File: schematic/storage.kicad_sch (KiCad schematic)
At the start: 0 parts

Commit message: revised schematic into sheets for easier design. Looks much better.
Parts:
- added JP1, JP2: SolderJumper_2_Open, symbol Jumper:SolderJumper_2_Open
- added U2: 27C256, Package_DIP:DIP-28_W15.24mm, symbol Memory_EPROM:27C256
- added U3, U4: SCM2114AL, symbol Vintage_PC_RAM:SCM2114AL
- added WJ4, WJ5: Jumper_2_Bridged_32K_ROM, symbol Jumper:Jumper_2_Bridged
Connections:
- new net: JP2.2 (B), U2.23 (A11), WJ5.2 (B)
- new net: JP1.1 (A), U2.20 (~{CE}), WJ4.1 (A)
- new net +5VD: U2.1 (VPP), U2.26 (A13), U2.27 (A14), U2.28 (VCC), U3.18 (VCC), U4.18 (VCC)
- new net A11: JP1.2 (B), WJ5.1 (A)
- new net A12: JP2.1 (A), U2.2 (A12)
- new net D0: U2.11 (D0)
- new net D1: U2.12 (D1)
- new net D2: U2.13 (D2)
- new net D3: U2.15 (D3)
- new net D4: U2.16 (D4), U4.14 (D0)
- new net D5: U2.17 (D5)
- new net D6: U2.18 (D6)
- new net D7: U2.19 (D7)
- new net U5_O0: U2.22 (~{OE}), WJ4.2 (B)

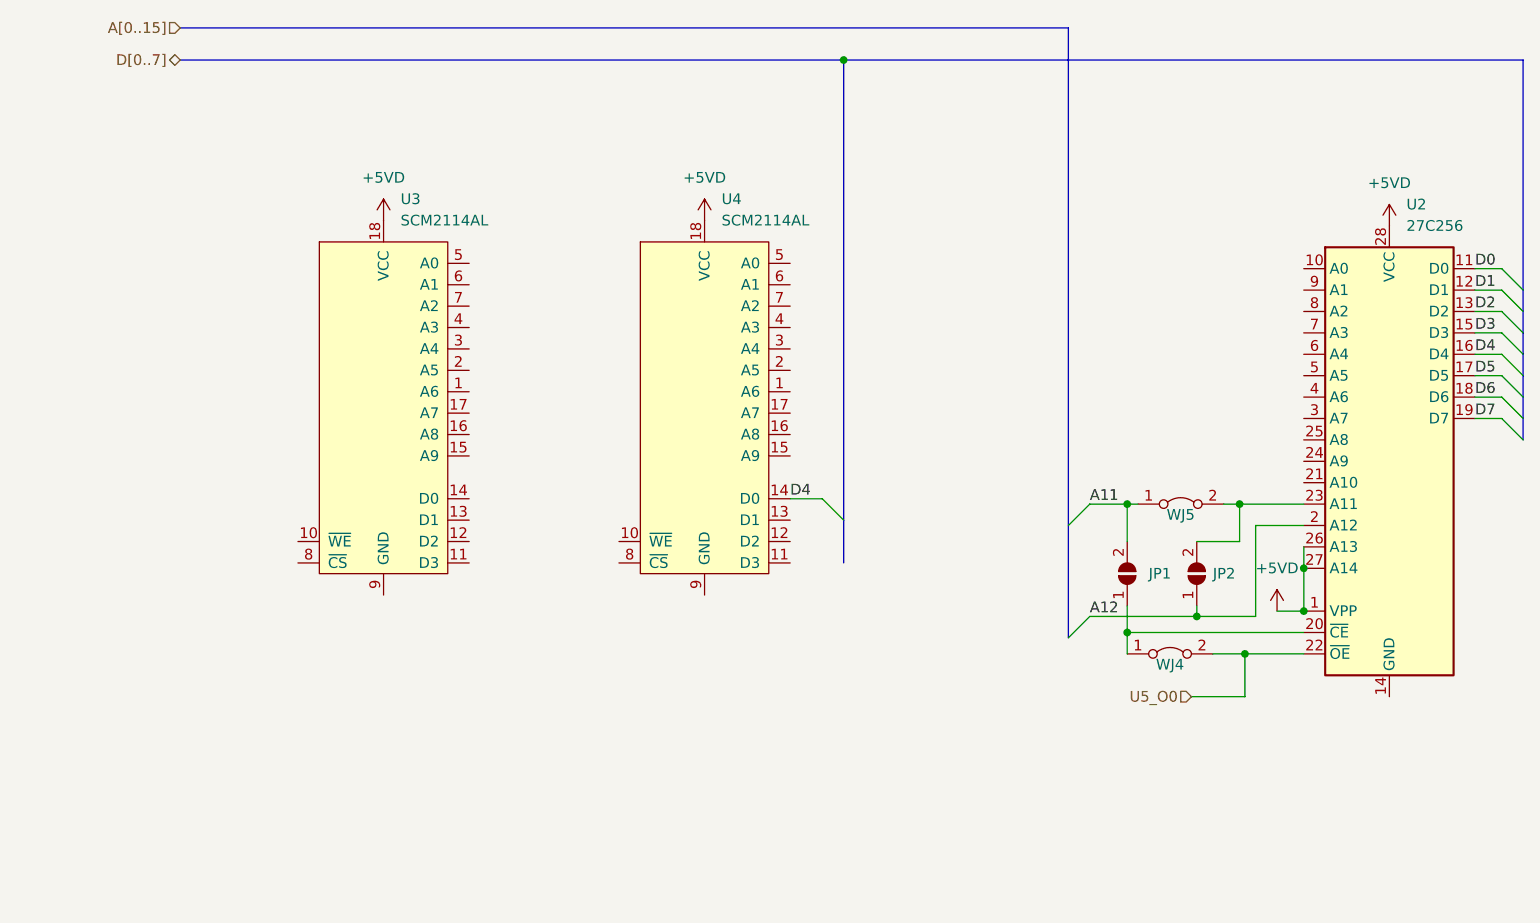
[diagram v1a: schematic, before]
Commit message: worked on the z80 trace up to and including pin 15.
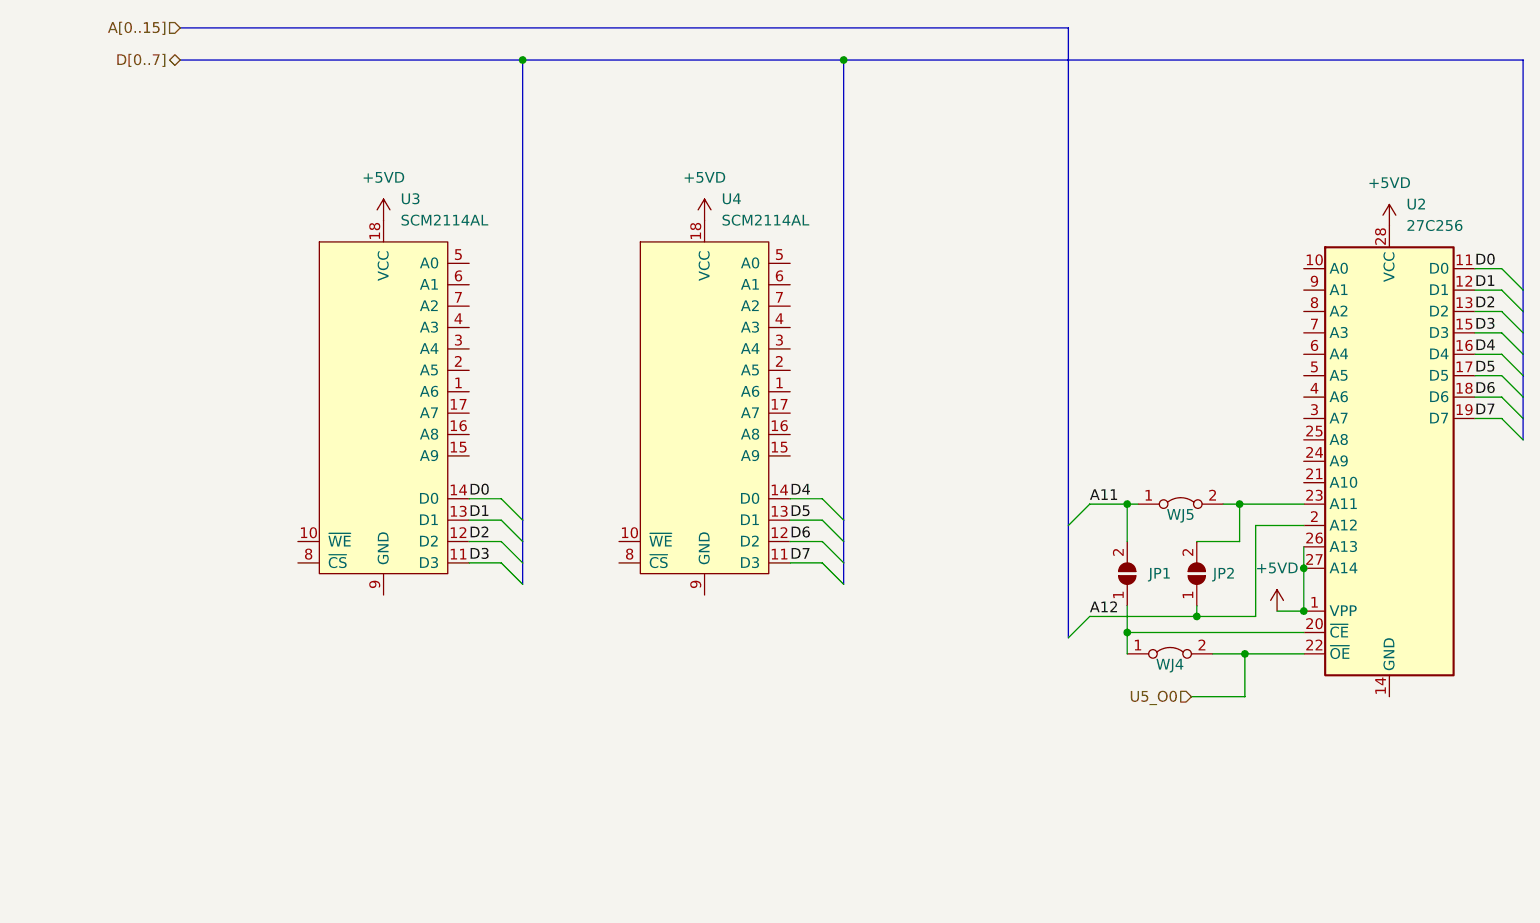
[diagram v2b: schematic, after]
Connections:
- net D0: now also U3.14 (D0)
- net D1: now also U3.13 (D1)
- net D2: now also U3.12 (D2)
- net D3: now also U3.11 (D3)
- net D5: now also U4.13 (D1)
- net D6: now also U4.12 (D2)
- net D7: now also U4.11 (D3)
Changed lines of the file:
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@@
   (junction (at 159.385 31.75) (diameter 0) (color 0 0 0 0)
   )
+  (junction (at 121.285 31.75) (diameter 0) (color 0 0 0 0)
+  )
   (junction (at 193.04 84.455) (diameter 0) (color 0 0 0 0)
   )
@@
     (stroke (width 0) (type default) (color 0 0 0 0))
   )
+  (bus_entry (at 118.745 83.82) (size 2.54 2.54)
+    (stroke (width 0) (type default) (color 0 0 0 0))
+  )
+  (bus_entry (at 118.745 91.44) (size 2.54 2.54)
+    (stroke (width 0) (type default) (color 0 0 0 0))
+  )
+  (bus_entry (at 118.745 86.36) (size 2.54 2.54)
+    (stroke (width 0) (type default) (color 0 0 0 0))
+  )
   (bus_entry (at 237.49 61.595) (size 2.54 2.54)
     (stroke (width 0) (type default) (color 0 0 0 0))
@@
     (stroke (width 0) (type default) (color 0 0 0 0))
   )
+  (bus_entry (at 156.845 91.44) (size 2.54 2.54)
+    (stroke (width 0) (type default) (color 0 0 0 0))
+  )
   (bus_entry (at 237.49 59.055) (size 2.54 2.54)
     (stroke (width 0) (type default) (color 0 0 0 0))
@@
     (stroke (width 0) (type default) (color 0 0 0 0))
   )
+  (bus_entry (at 156.845 88.9) (size 2.54 2.54)
+    (stroke (width 0) (type default) (color 0 0 0 0))
+  )
   (bus_entry (at 156.845 83.82) (size 2.54 2.54)
     (stroke (width 0) (type default) (color 0 0 0 0))
   )
+  (bus_entry (at 156.845 86.36) (size 2.54 2.54)
+    (stroke (width 0) (type default) (color 0 0 0 0))
+  )
+  (bus_entry (at 118.745 88.9) (size 2.54 2.54)
+    (stroke (width 0) (type default) (color 0 0 0 0))
+  )
   (bus_entry (at 237.49 56.515) (size 2.54 2.54)
     (stroke (width 0) (type default) (color 0 0 0 0))
@@
     (stroke (width 0) (type default) (color 0 0 0 0))
   )
+  (bus (pts (xy 121.285 86.36) (xy 121.285 88.9))
+    (stroke (width 0) (type default) (color 0 0 0 0))
+  )
+  (bus (pts (xy 121.285 91.44) (xy 121.285 93.98))
+    (stroke (width 0) (type default) (color 0 0 0 0))
+  )
   (bus (pts (xy 186.055 86.995) (xy 186.055 100.33))
     (stroke (width 0) (type default) (color 0 0 0 0))
@@
     (stroke (width 0) (type default) (color 0 0 0 0))
   )
+  (bus (pts (xy 121.285 88.9) (xy 121.285 91.44))
+    (stroke (width 0) (type default) (color 0 0 0 0))
+  )
   (wire (pts (xy 188.595 84.455) (xy 193.04 84.455))
     (stroke (width 0) (type default) (color 0 0 0 0))
@@
     (stroke (width 0) (type default) (color 0 0 0 0))
   )
-  (bus (pts (xy 159.385 86.36) (xy 159.385 91.44))
+  (bus (pts (xy 159.385 86.36) (xy 159.385 88.9))
     (stroke (width 0) (type default) (color 0 0 0 0))
   )
@@
     (stroke (width 0) (type default) (color 0 0 0 0))
   )
+  (bus (pts (xy 121.285 31.75) (xy 121.285 86.36))
+    (stroke (width 0) (type default) (color 0 0 0 0))
+  )
   (wire (pts (xy 203.2 102.235) (xy 207.01 102.235))
     (stroke (width 0) (type default) (color 0 0 0 0))
   )
+  (bus (pts (xy 159.385 91.44) (xy 159.385 93.98))
+    (stroke (width 0) (type default) (color 0 0 0 0))
+  )
   (wire (pts (xy 193.04 96.52) (xy 193.04 99.695))
     (stroke (width 0) (type default) (color 0 0 0 0))
@@
     (stroke (width 0) (type default) (color 0 0 0 0))
   )
+  (wire (pts (xy 153.035 86.36) (xy 156.845 86.36))
+    (stroke (width 0) (type default) (color 0 0 0 0))
+  )
   (wire (pts (xy 201.295 96.52) (xy 201.295 97.79))
     (stroke (width 0) (type default) (color 0 0 0 0))
   )
+  (bus (pts (xy 121.285 31.75) (xy 159.385 31.75))
+    (stroke (width 0) (type default) (color 0 0 0 0))
+  )
   (wire (pts (xy 234.315 56.515) (xy 237.49 56.515))
     (stroke (width 0) (type default) (color 0 0 0 0))
@@
     (stroke (width 0) (type default) (color 0 0 0 0))
   )
+  (wire (pts (xy 153.035 88.9) (xy 156.845 88.9))
+    (stroke (width 0) (type default) (color 0 0 0 0))
+  )
   (bus (pts (xy 80.645 27.94) (xy 186.055 27.94))
     (stroke (width 0) (type default) (color 0 0 0 0))
   )
+  (bus (pts (xy 159.385 88.9) (xy 159.385 91.44))
+    (stroke (width 0) (type default) (color 0 0 0 0))
+  )
   (wire (pts (xy 193.04 84.455) (xy 194.31 84.455))
     (stroke (width 0) (type default) (color 0 0 0 0))
@@
     (stroke (width 0) (type default) (color 0 0 0 0))
   )
+  (wire (pts (xy 114.935 88.9) (xy 118.745 88.9))
+    (stroke (width 0) (type default) (color 0 0 0 0))
+  )
+  (wire (pts (xy 114.935 91.44) (xy 118.745 91.44))
+    (stroke (width 0) (type default) (color 0 0 0 0))
+  )
+  (wire (pts (xy 114.935 86.36) (xy 118.745 86.36))
+    (stroke (width 0) (type default) (color 0 0 0 0))
+  )
   (wire (pts (xy 234.315 61.595) (xy 237.49 61.595))
     (stroke (width 0) (type default) (color 0 0 0 0))
@@
     (stroke (width 0) (type default) (color 0 0 0 0))
   )
-  (bus (pts (xy 80.645 31.75) (xy 159.385 31.75))
+  (bus (pts (xy 80.645 31.75) (xy 121.285 31.75))
     (stroke (width 0) (type default) (color 0 0 0 0))
   )
@@
     (stroke (width 0) (type default) (color 0 0 0 0))
   )
+  (wire (pts (xy 114.935 83.82) (xy 118.745 83.82))
+    (stroke (width 0) (type default) (color 0 0 0 0))
+  )
   (bus (pts (xy 240.03 59.055) (xy 240.03 61.595))
     (stroke (width 0) (type default) (color 0 0 0 0))
   )
+  (wire (pts (xy 153.035 91.44) (xy 156.845 91.44))
+    (stroke (width 0) (type default) (color 0 0 0 0))
+  )
   (bus (pts (xy 240.03 71.755) (xy 240.03 74.295))
     (stroke (width 0) (type default) (color 0 0 0 0))
@@
     (effects (font (size 1.27 1.27)) (justify left bottom))
   )
+  (label "D3" (at 114.935 91.44 0)
+    (effects (font (size 1.27 1.27)) (justify left bottom))
+  )
   (label "D7" (at 234.315 74.295 0)
     (effects (font (size 1.27 1.27)) (justify left bottom))
@@
     (effects (font (size 1.27 1.27)) (justify left bottom))
   )
+  (label "D5" (at 153.035 86.36 0)
+    (effects (font (size 1.27 1.27)) (justify left bottom))
+  )
   (label "A12" (at 188.595 97.79 0)
     (effects (font (size 1.27 1.27)) (justify left bottom))
   )
+  (label "D7" (at 153.035 91.44 0)
+    (effects (font (size 1.27 1.27)) (justify left bottom))
+  )
   (label "D4" (at 153.035 83.82 0)
     (effects (font (size 1.27 1.27)) (justify left bottom))
@@
     (effects (font (size 1.27 1.27)) (justify left bottom))
   )
+  (label "D6" (at 153.035 88.9 0)
+    (effects (font (size 1.27 1.27)) (justify left bottom))
+  )
   (label "A11" (at 188.595 84.455 0)
     (effects (font (size 1.27 1.27)) (justify left bottom))
   )
+  (label "D1" (at 114.935 86.36 0)
+    (effects (font (size 1.27 1.27)) (justify left bottom))
+  )
+  (label "D0" (at 114.935 83.82 0)
+    (effects (font (size 1.27 1.27)) (justify left bottom))
+  )
   (label "D3" (at 234.315 64.135 0)
     (effects (font (size 1.27 1.27)) (justify left bottom))
@@
     (effects (font (size 1.27 1.27)) (justify left bottom))
   )
+  (label "D2" (at 114.935 88.9 0)
+    (effects (font (size 1.27 1.27)) (justify left bottom))
+  )

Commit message: changed all vintage library names to better represent future ideas. Removed parts not needed... for now. Updated schmematic symbols.
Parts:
- U3, U4: symbol Vintage_PC_RAM:SCM2114AL -> Vintage_RAM:SCM2114AL
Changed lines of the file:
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@@
     (effects (font (size 1.27 1.27)) (justify right))
   )
-  (symbol (lib_id "Vintage_PC_RAM:SCM2114AL") (at 104.775 57.15 0) (unit 1)
+  (symbol (lib_id "Vintage_RAM:SCM2114AL") (at 104.775 57.15 0) (unit 1)
     (in_bom yes) (on_board yes) (fields_autoplaced)
     (property "Reference" "U3" (id 0) (at 106.7944 48.26 0)
@@
     (pin "1")
   )
-  (symbol (lib_id "Vintage_PC_RAM:SCM2114AL") (at 142.875 57.15 0) (unit 1)
+  (symbol (lib_id "Vintage_RAM:SCM2114AL") (at 142.875 57.15 0) (unit 1)
     (in_bom yes) (on_board yes) (fields_autoplaced)
     (property "Reference" "U4" (id 0) (at 144.8944 48.26 0)
